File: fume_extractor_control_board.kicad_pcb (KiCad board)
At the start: 2 copper layers, 58 x 58 mm, 39 parts, among them J1 Noctua Fan Header, J2 Barrel_Jack_MountingPin, J3 SWD Header, SW1 RESET, U1 MP2338GTL-Z, U2 STM32F030RCTx, Y1 8MHz

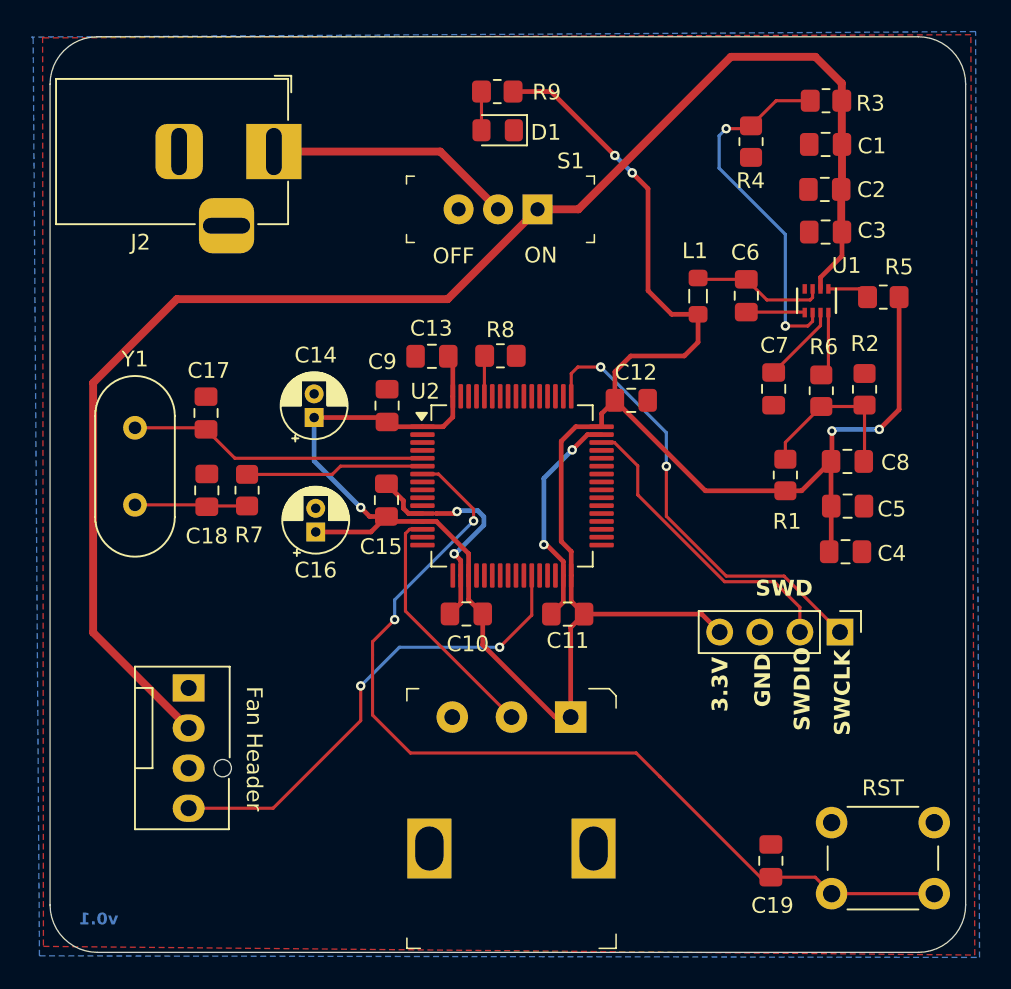
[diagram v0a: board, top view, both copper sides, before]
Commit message: Adjusted some traces
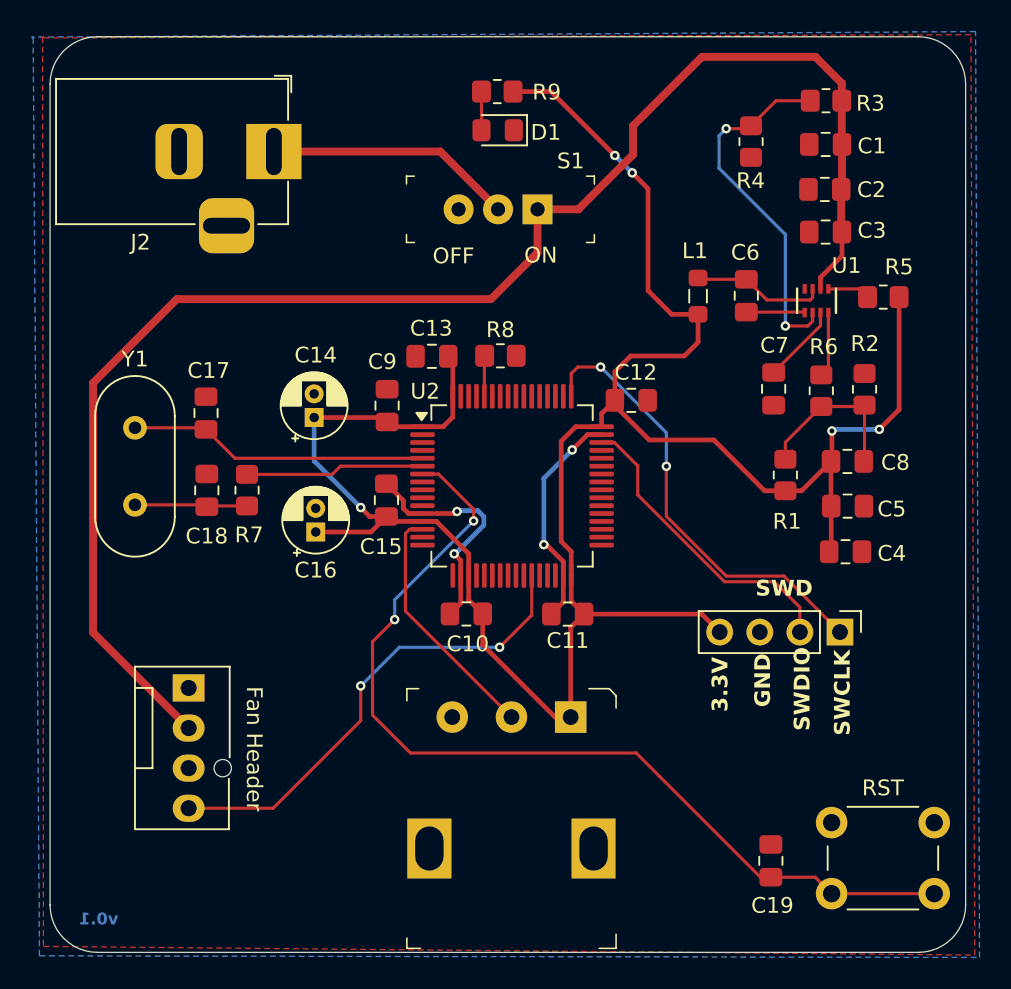
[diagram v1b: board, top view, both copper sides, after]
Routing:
- net +12V: track 94.7 -> 97.4 mm
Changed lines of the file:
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@@
+	)
+	(segment
+		(start 153.69 84.31)
+		(end 157.15 80.85)
+		(width 0.5)
+		(layer "F.Cu")
+		(net 2)
+	)
+	(segment
+		(start 170.3375 85.7)
+		(end 170.3875 85.75)
+		(width 0.5)
+		(layer "F.Cu")
+		(net 2)
+	)
+	(segment
+		(start 170.375 80.1875)
+		(end 170.3875 80.2)
+		(width 0.5)
+		(layer "F.Cu")
+		(net 2)
+	)
+	(segment
+		(start 170.3875 87.2625)
+		(end 170.3875 85.75)
+		(width 0.3)
+		(layer "F.Cu")
+		(net 2)
+	)
+	(segment
+		(start 157.15 80.85)
+		(end 157.15 79.02)
+		(width 0.5)
+		(layer "F.Cu")
+		(net 2)
+	)
+	(segment
+		(start 148.15 90)
+		(end 151.1 87.05)
+		(width 0.5)
+		(layer "F.Cu")
+		(net 2)
+	)
+	(segment
+		(start 169.024999 89.3514)
+		(end 169.024999 88.625001)
+		(width 0.3)
+		(layer "F.Cu")
+		(net 2)
+	)
+	(segment
+		(start 161.52 74.65)
+		(end 168.7 74.65)
+		(width 0.5)
+		(layer "F.Cu")
+		(net 2)
+	)
+	(segment
+		(start 170.375 76.325)
+		(end 170.375 77.43)
+		(width 0.5)
+		(layer "F.Cu")
+		(net 2)
+	)
+	(segment
+		(start 122.95 95.3)
+		(end 128.25 90)
+		(width 0.5)
+		(layer "F.Cu")
+		(net 2)
+	)
+	(segment
+		(start 170.3875 83)
+		(end 170.3375 83.05)
+		(width 0.5)
+		(layer "F.Cu")
+		(net 2)
+	)
+	(segment
+		(start 170.375 77.43)
+		(end 170.375 80.1875)
+		(width 0.5)
+		(layer "F.Cu")
+		(net 2)
 	)
 	(segment
@@
 	)
 	(segment
+		(start 151.1 87.05)
+		(end 151.1 84.31)
+		(width 0.5)
+		(layer "F.Cu")
+		(net 2)
+	)
+	(segment
+		(start 122.95 111.12)
+		(end 122.95 95.3)
+		(width 0.5)
+		(layer "F.Cu")
+		(net 2)
+	)
+	(segment
+		(start 129 117.17)
+		(end 122.95 111.12)
+		(width 0.5)
+		(layer "F.Cu")
+		(net 2)
+	)
+	(segment
+		(start 170.3375 83.05)
+		(end 170.3375 85.7)
+		(width 0.5)
+		(layer "F.Cu")
+		(net 2)
+	)
+	(segment
+		(start 169.024999 88.625001)
+		(end 170.3875 87.2625)
+		(width 0.3)
+		(layer "F.Cu")
+		(net 2)
+	)
+	(segment
+		(start 128.25 90)
+		(end 148.15 90)
+		(width 0.5)
+		(layer "F.Cu")
+		(net 2)
+	)
+	(segment
+		(start 157.15 79.02)
+		(end 161.52 74.65)
+		(width 0.5)
+		(layer "F.Cu")
+		(net 2)
+	)
+	(segment
+		(start 170.3875 80.2)
+		(end 170.3875 83)
+		(width 0.5)
+		(layer "F.Cu")
+		(net 2)
+	)
+	(segment
 		(start 168.7 74.65)
 		(end 170.375 76.325)
@@
 	)
 	(segment
-		(start 170.3375 85.7)
-		(end 170.3875 85.75)
-		(width 0.5)
-		(layer "F.Cu")
-		(net 2)
-	)
-	(segment
-		(start 170.375 80.1875)
-		(end 170.3875 80.2)
-		(width 0.5)
-		(layer "F.Cu")
-		(net 2)
-	)
-	(segment
-		(start 170.3875 87.2625)
-		(end 170.3875 85.75)
-		(width 0.3)
-		(layer "F.Cu")
-		(net 2)
-	)
-	(segment
-		(start 129 117.17)
-		(end 122.95 111.12)
-		(width 0.5)
-		(layer "F.Cu")
-		(net 2)
-	)
-	(segment
-		(start 163.35 74.65)
-		(end 168.7 74.65)
-		(width 0.5)
-		(layer "F.Cu")
-		(net 2)
-	)
-	(segment
-		(start 169.024999 89.3514)
-		(end 169.024999 88.625001)
-		(width 0.3)
-		(layer "F.Cu")
-		(net 2)
-	)
-	(segment
-		(start 170.375 76.325)
-		(end 170.375 77.43)
-		(width 0.5)
-		(layer "F.Cu")
-		(net 2)
-	)
-	(segment
-		(start 170.3875 83)
-		(end 170.3375 83.05)
-		(width 0.5)
-		(layer "F.Cu")
-		(net 2)
-	)
-	(segment
-		(start 170.375 77.43)
-		(end 170.375 80.1875)
-		(width 0.5)
-		(layer "F.Cu")
-		(net 2)
-	)
-	(segment
-		(start 145.41 90)
-		(end 151.1 84.31)
-		(width 0.5)
-		(layer "F.Cu")
-		(net 2)
-	)
-	(segment
-		(start 170.3375 83.05)
-		(end 170.3375 85.7)
-		(width 0.5)
-		(layer "F.Cu")
-		(net 2)
-	)
-	(segment
-		(start 169.024999 88.625001)
-		(end 170.3875 87.2625)
-		(width 0.3)
-		(layer "F.Cu")
-		(net 2)
-	)
-	(segment
-		(start 128.25 90)
-		(end 145.41 90)
-		(width 0.5)
-		(layer "F.Cu")
-		(net 2)
-	)
-	(segment
-		(start 122.95 95.3)
-		(end 128.25 90)
-		(width 0.5)
-		(layer "F.Cu")
-		(net 2)
-	)
-	(segment
-		(start 170.3875 80.2)
-		(end 170.3875 83)
-		(width 0.5)
-		(layer "F.Cu")
-		(net 2)
-	)
-	(segment
-		(start 153.69 84.31)
-		(end 163.35 74.65)
-		(width 0.5)
-		(layer "F.Cu")
-		(net 2)
-	)
-	(segment
-		(start 122.95 111.12)
-		(end 122.95 95.3)
-		(width 0.5)
-		(layer "F.Cu")
-		(net 2)
-	)
-	(segment
 		(start 153.235 107.505)
 		(end 153.235 105.985)
@@
 	)
 	(segment
+		(start 166.8 102.14)
+		(end 165.49 102.14)
+		(width 0.3)
+		(layer "F.Cu")
+		(net 3)
+	)
+	(segment
 		(start 145.735 97.465)
 		(end 145.735 96.155)
@@
 	)
 	(segment
+		(start 158.18 98.92)
+		(end 156.0025 96.7425)
+		(width 0.3)
+		(layer "F.Cu")
+		(net 3)
+	)
+	(segment
 		(start 153.2 110.8)
 		(end 154.05 109.95)
@@
 	)
 	(segment
-		(start 156.0025 96.41)
-		(end 161.7325 102.14)
-		(width 0.3)
-		(layer "F.Cu")
-		(net 3)
-	)
-	(segment
 		(start 169.705 105.87)
 		(end 169.575 106)
@@
 	)
 	(segment
-		(start 161.7325 102.14)
-		(end 166.8 102.14)
+		(start 156.0025 96.7425)
+		(end 156.0025 96.41)
+		(width 0.3)
+		(layer "F.Cu")
+		(net 3)
+	)
+	(segment
+		(start 162.27 98.92)
+		(end 158.18 98.92)
 		(width 0.3)
 		(layer "F.Cu")
@@
 		(width 0.3)
 		(layer "F.Cu")
+		(net 3)
+	)
+	(segment
+		(start 165.49 102.14)
+		(end 162.27 98.92)
+		(width 0.3)
+		(layer "F.Cu")
